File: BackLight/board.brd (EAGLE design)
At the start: 100 x 80 mm, 16 parts

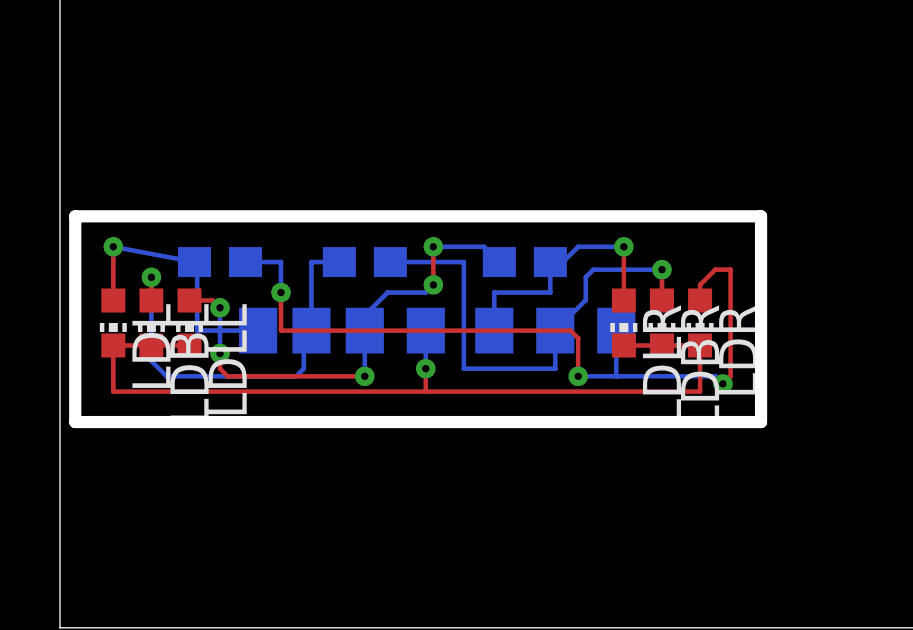
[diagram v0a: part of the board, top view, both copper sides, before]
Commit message: Fix light board. Fix carsystem board.
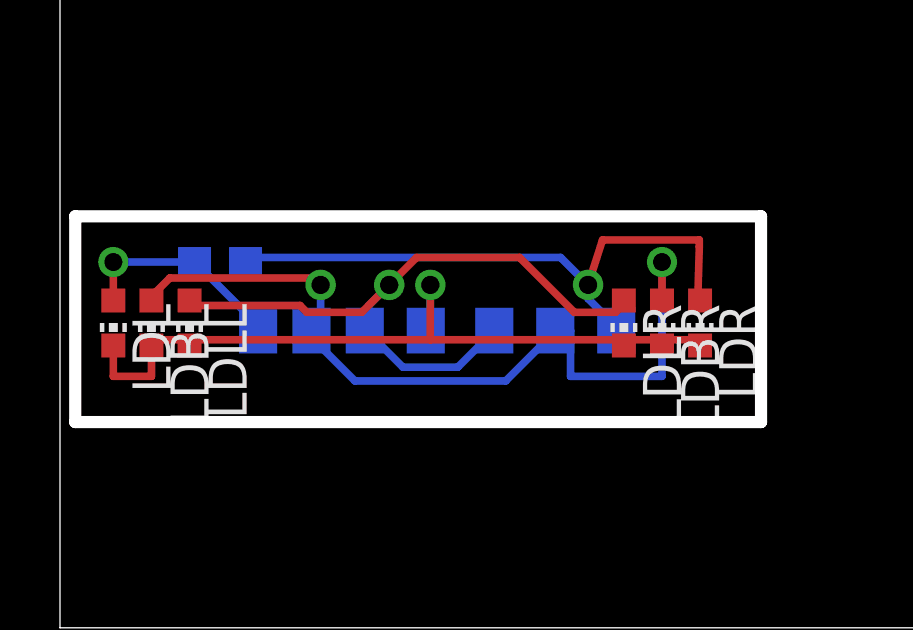
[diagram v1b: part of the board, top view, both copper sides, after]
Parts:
- removed R2, R3: 0, SparkFun-Resistors:0603
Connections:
- removed net N$5: LDLR.A, LR.1, R3.2
- removed net N$6: BR.1, LDBR.A, R2.2
- net N$3: now also BR.1, LDBR.A; no longer R2.1
- net N$4: now also LDLR.A, LR.1; no longer R3.1
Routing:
- net N$6: track 16.2 -> 0.00 mm, vias 1 -> 0
- net N$3: track 13.6 -> 27.8 mm, vias 1 -> 2
- net N$5: track 8.60 -> 0.00 mm, vias 1 -> 0
- net N$4: track 16.5 -> 23.6 mm, vias 5 -> 1
- net N$7: track 26.9 -> 20.6 mm, vias 3 -> 1
- net N$1: track 29.7 -> 26.0 mm
- net N$2: track 8.95 -> 7.17 mm
